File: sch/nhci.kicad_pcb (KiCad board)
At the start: 4 copper layers, 33 parts, among them IC1 74LVC8T245RHLRG4, IC2 74LVC8T245RHLRG4, IC3 74LVC8T245RHLRG4, IC4 74LVC8T245RHLRG4, IC5 74LVC8T245RHLRG4, IC6 MAX3421EEHJ+, SW1 SW_Push_Open, U1 PCMCIA_BOARD, U2 iCE40-HX8K-CT256, U3 N25Q032A13EF440F, Y1 ECS-5032MV-120-BM-TR

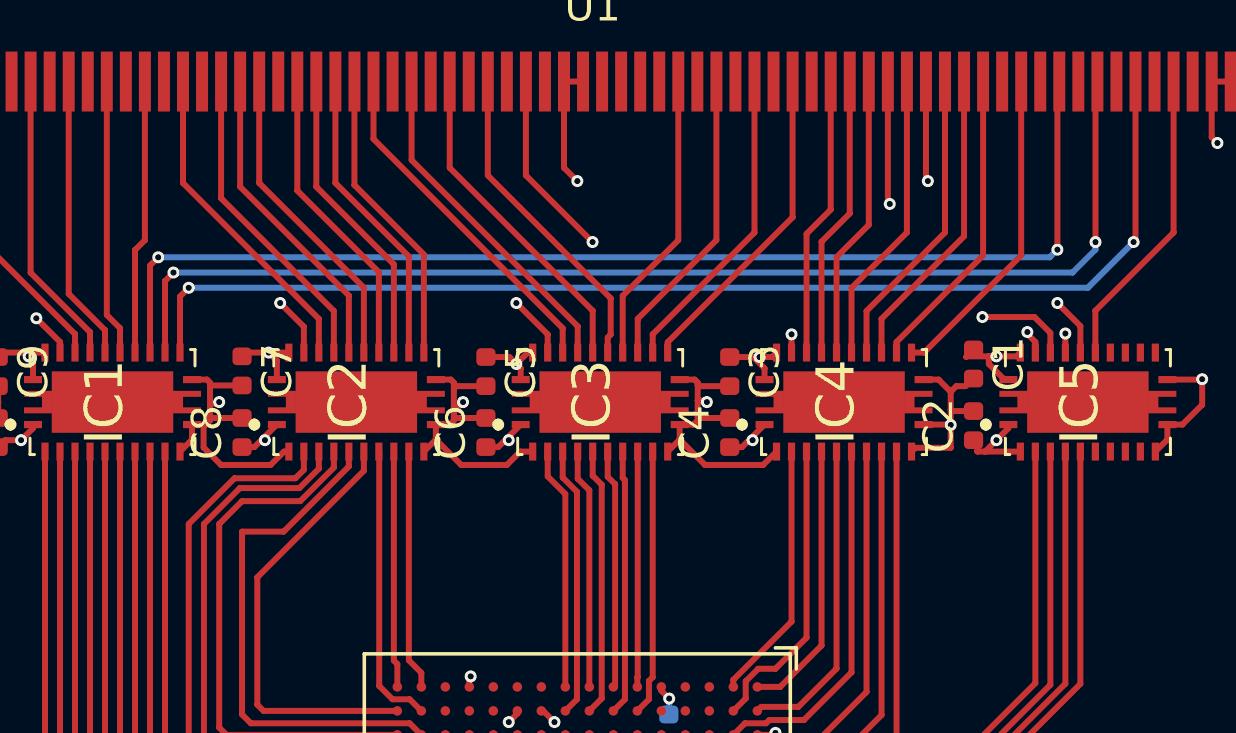
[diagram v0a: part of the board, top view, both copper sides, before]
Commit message: Add pullup resistors
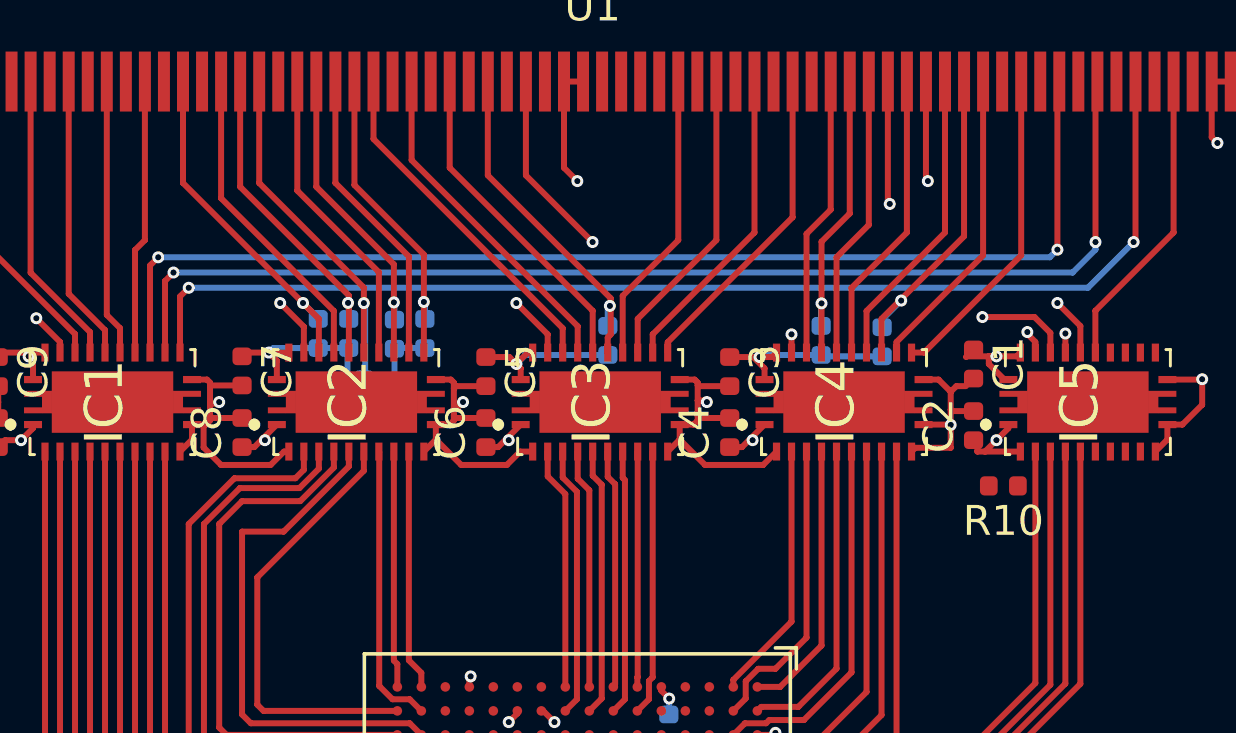
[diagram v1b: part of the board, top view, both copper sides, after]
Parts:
- added R10: 10k, Resistor_SMD:R_0402_1005Metric, F.Cu at (79.5, 111.8)
- added R2: 10k, Resistor_SMD:R_0402_1005Metric, B.Cu at (56.6, 106.7)
- added R3: 10k, Resistor_SMD:R_0402_1005Metric, B.Cu at (57.7, 106.7)
- added R4: 10k, Resistor_SMD:R_0402_1005Metric, B.Cu at (75.4, 107.0)
- added R5: 10k, Resistor_SMD:R_0402_1005Metric, B.Cu at (59.2, 106.7)
- added R6: 10k, Resistor_SMD:R_0402_1005Metric, B.Cu at (60.2, 106.7)
- added R7: 10k, Resistor_SMD:R_0402_1005Metric, B.Cu at (58.2, 108.7)
- added R8: 10k, Resistor_SMD:R_0402_1005Metric, B.Cu at (66.3, 106.9)
- added R9: 100k, Resistor_SMD:R_0402_1005Metric, B.Cu at (73.4, 106.9)
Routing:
- net +5V: track 57.8 -> 73.5 mm
- net /P_OE: track 10.5 -> 13.0 mm, vias 0 -> 1
- net /P_REG: track 10.2 -> 11.3 mm, vias 0 -> 1
- net /P_RESET: track 9.42 -> 10.2 mm, vias 0 -> 1
- net /P_CE1: track 10.9 -> 11.7 mm, vias 0 -> 1
- net /P_WE: track 10.8 -> 11.5 mm, vias 0 -> 1
- net /P_IORD: track 10.1 -> 10.7 mm, vias 0 -> 1
- net /P_IOWR: track 9.99 -> 10.6 mm, vias 0 -> 1
- net /P_CE2: track 10.5 -> 11.1 mm, vias 0 -> 1

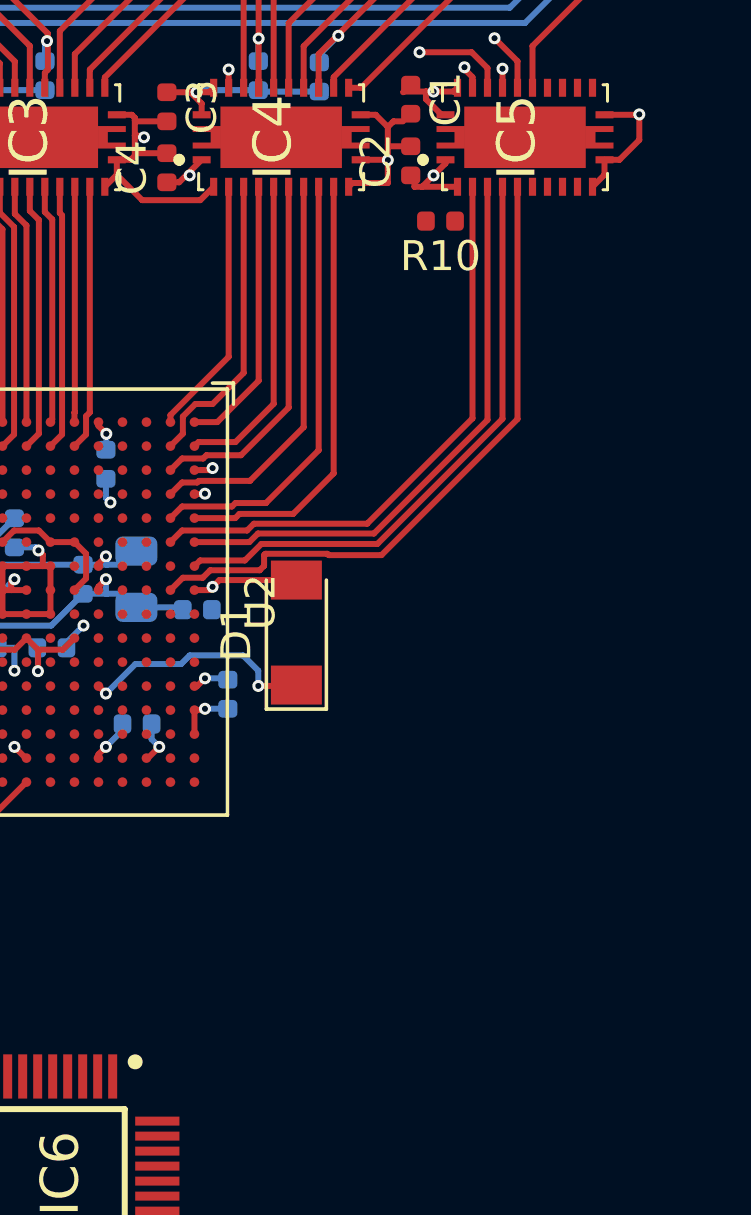
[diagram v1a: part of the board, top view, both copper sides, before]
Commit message: Add voltage regulator
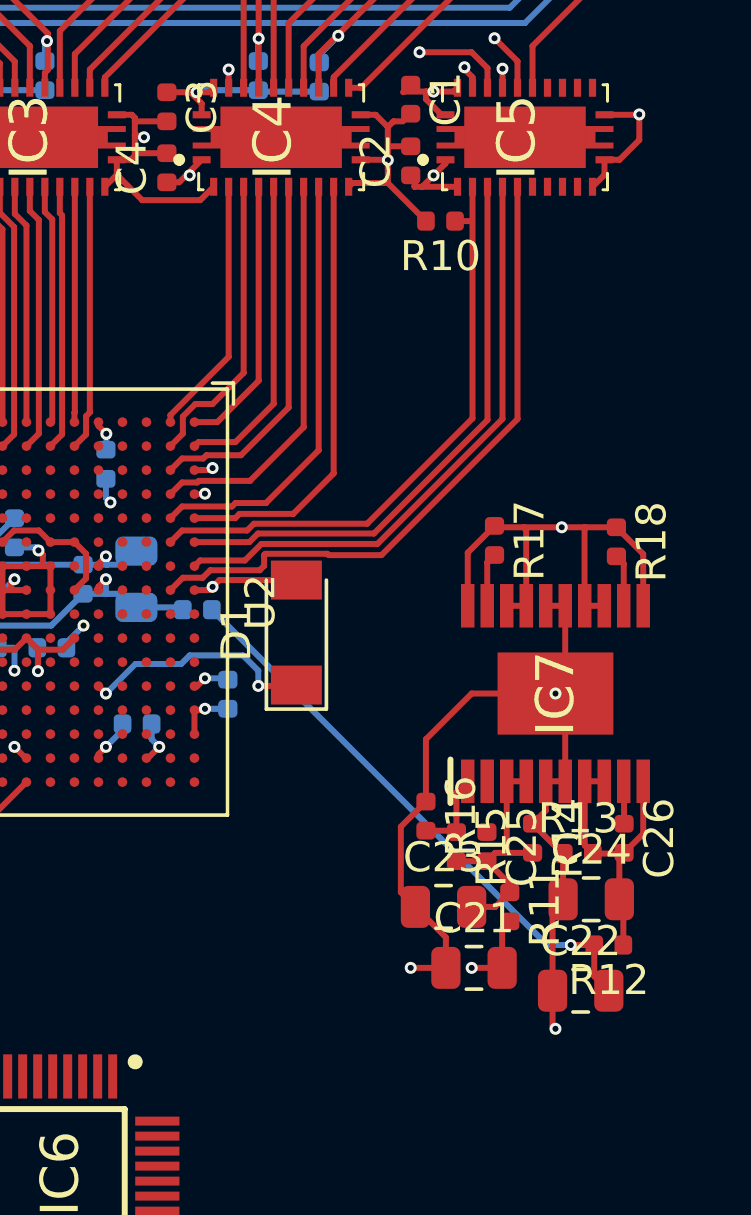
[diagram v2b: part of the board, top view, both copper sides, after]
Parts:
- added C21: 10uF, Capacitor_SMD:C_0805_2012Metric, F.Cu at (80.6, 136.7)
- added C22: 10uF, Capacitor_SMD:C_0805_2012Metric, F.Cu at (84.2, 137.4)
- added C23: 10uF, Capacitor_SMD:C_0805_2012Metric, F.Cu at (79.6, 134.6)
- added C24: 4.7uF, Capacitor_SMD:C_0805_2012Metric, F.Cu at (84.5, 134.4)
- added C25: 10nF, Capacitor_SMD:C_0402_1005Metric, F.Cu at (81.0, 132.6)
- added C26: 10nF, Capacitor_SMD:C_0402_1005Metric, F.Cu at (85.6, 132.3)
- added IC7: LT3030IFE#TRPBF, LT3030IFE#TRPBF:SOP65P640X120-21N, F.Cu at (83.3, 127.5)
- added R11: 0.1, Resistor_SMD:R_0402_1005Metric, F.Cu at (81.8, 134.6)
- added R12: 0.1, Resistor_SMD:R_0402_1005Metric, F.Cu at (85.1, 135.9)
- added R13: 100, Resistor_SMD:R_0402_1005Metric, F.Cu at (84.1, 132.8)
- added R14: 100, Resistor_SMD:R_0402_1005Metric, F.Cu at (82.5, 132.3)
- added R15: 357k, Resistor_SMD:R_0402_1005Metric, F.Cu at (80.0, 132.6)
- added R16: 210k, Resistor_SMD:R_0402_1005Metric, F.Cu at (79.0, 131.6)
- added R17: 1M, Resistor_SMD:R_0402_1005Metric, F.Cu at (81.3, 122.4)
- added R18: 1M, Resistor_SMD:R_0402_1005Metric, F.Cu at (85.3, 122.5)
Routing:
- net +5V: track 73.5 -> 106.9 mm, vias 6 -> 7
- net GND: track 80.7 -> 113.8 mm, vias 30 -> 33
- net +1V2: track 0.00 -> 19.1 mm, vias 0 -> 1
- net +3V3: track 95.8 -> 108.4 mm, vias 23 -> 24
- net Net-(C24-Pad2): track 0.00 -> 10.1 mm
- net Net-(C23-Pad2): track 0.00 -> 8.55 mm
- net Net-(IC7-Pad1): track 0.00 -> 2.88 mm
- net Net-(IC7-Pad19): track 0.00 -> 1.79 mm
- net Net-(IC7-Pad12): track 0.00 -> 1.75 mm
- net Net-(C26-Pad1): track 0.00 -> 1.42 mm
- net F_READY: track 19.5 -> 20.1 mm

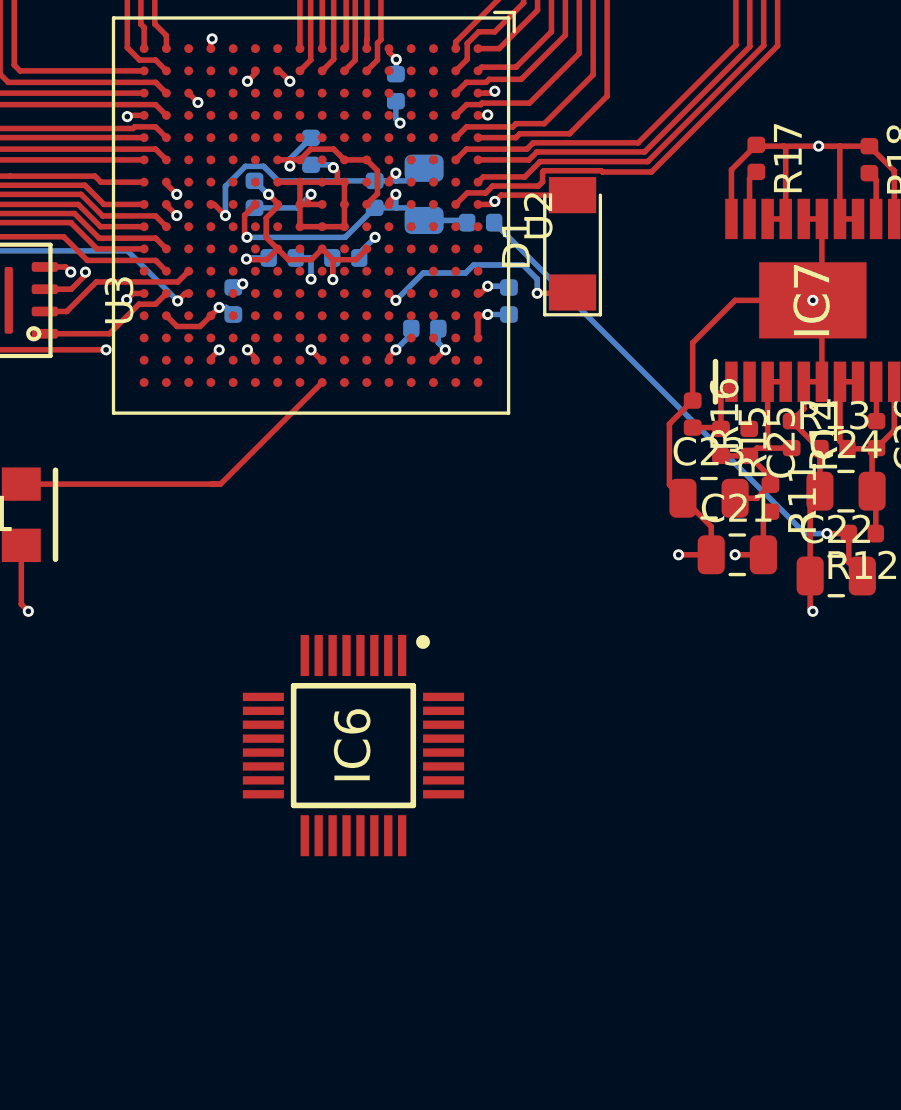
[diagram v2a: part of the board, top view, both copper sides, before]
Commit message: Add usb controller
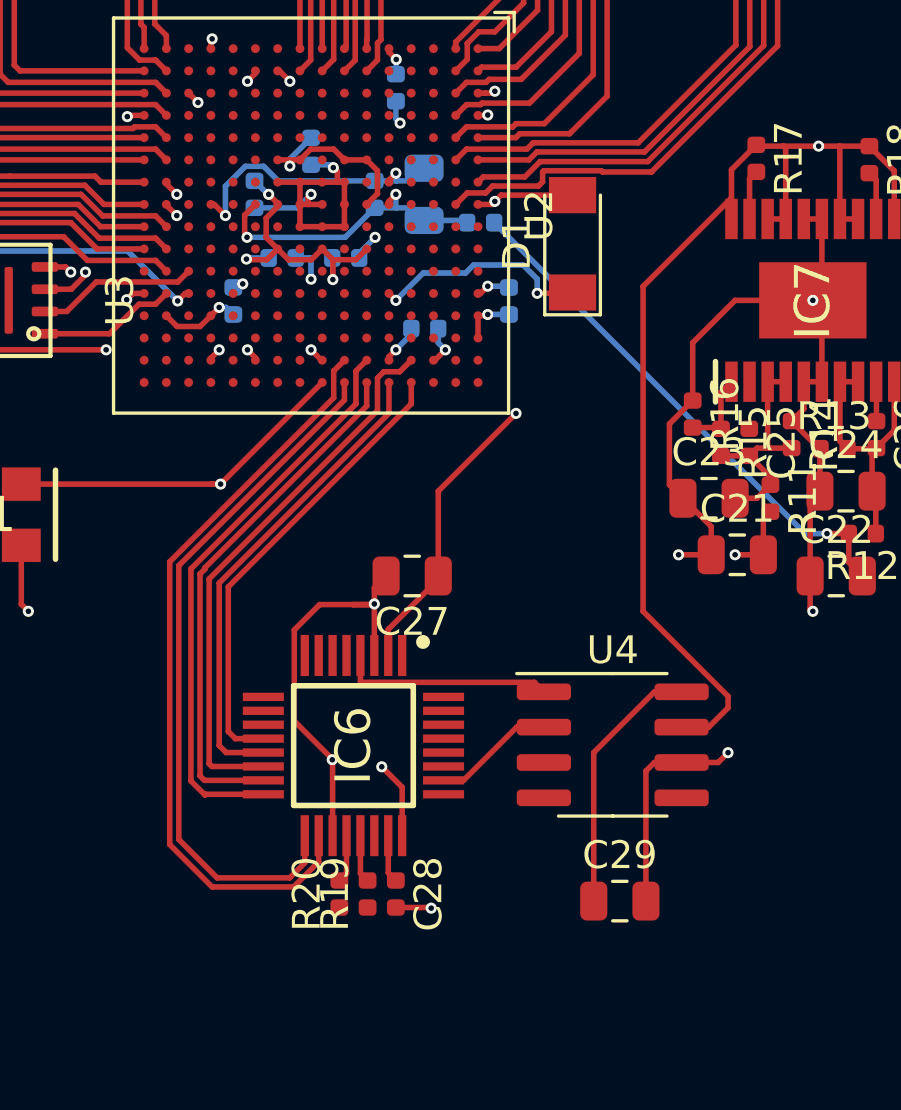
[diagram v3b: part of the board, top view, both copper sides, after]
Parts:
- added C27: 1uF, Capacitor_SMD:C_0805_2012Metric, F.Cu at (68.9, 137.4)
- added C28: 100nF, Capacitor_SMD:C_0402_1005Metric, F.Cu at (68.3, 148.8)
- added C29: 4.7uF, Capacitor_SMD:C_0805_2012Metric, F.Cu at (76.4, 149.1)
- added R19: 33, Resistor_SMD:R_0402_1005Metric, F.Cu at (67.3, 148.8)
- added R20: 33, Resistor_SMD:R_0402_1005Metric, F.Cu at (66.3, 148.8)
- added U4: LM3526M-H, Package_SO:SOIC-8_3.9x4.9mm_P1.27mm, F.Cu at (76.1, 143.5)
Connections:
- IC6 pad 12: Net-(IC6-Pad12) -> U_RES
- IC6 pad 13: Net-(IC6-Pad13) -> U_SCLK
- IC6 pad 14: Net-(IC6-Pad14) -> U_SS
- IC6 pad 15: Net-(IC6-Pad15) -> U_MISO
- IC6 pad 16: Net-(IC6-Pad16) -> U_MOSI
- IC6 pad 17: Net-(IC6-Pad17) -> U_GPX
- IC6 pad 18: Net-(IC6-Pad18) -> U_INT
- IC6 pad 19: Net-(IC6-Pad19) -> GND
- IC6 pad 2: Net-(IC6-Pad2) -> +3V3
- IC6 pad 23: Net-(IC6-Pad23) -> +3V3
- IC6 pad 24: Net-(IC6-Pad24) -> 12MHz
- IC6 pad 3: Net-(IC6-Pad3) -> GND
- U2 pad D15: Net-(U2-PadD15) -> U_SS
- U2 pad D16: Net-(U2-PadD16) -> U_RES
- U2 pad E16: Net-(U2-PadE16) -> U_SCLK
- U2 pad F15: Net-(U2-PadF15) -> U_MOSI
- U2 pad F16: Net-(U2-PadF16) -> U_MISO
- U2 pad G15: Net-(U2-PadG15) -> U_INT
- U2 pad G16: Net-(U2-PadG16) -> U_GPX
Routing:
- net U_INT: track 0.00 -> 27.3 mm
- net U_GPX: track 0.00 -> 25.2 mm
- net GND: track 113.8 -> 138.0 mm, vias 33 -> 37
- net +5V: track 106.9 -> 129.8 mm
- net U_MOSI: track 0.00 -> 20.6 mm
- net U_SS: track 0.00 -> 19.8 mm
- net U_MISO: track 0.00 -> 19.0 mm
- net U_SCLK: track 0.00 -> 17.3 mm
- net U_RES: track 0.00 -> 16.6 mm
- net 12MHz: track 12.6 -> 27.9 mm, vias 0 -> 2
- net +3V3: track 108.4 -> 120.7 mm, vias 24 -> 25
- net Net-(C29-Pad1): track 0.00 -> 9.40 mm
- net Net-(IC6-Pad4): track 0.00 -> 7.68 mm
- net Net-(IC6-Pad26): track 0.00 -> 4.40 mm
- net Net-(IC6-Pad20): track 0.00 -> 1.72 mm
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
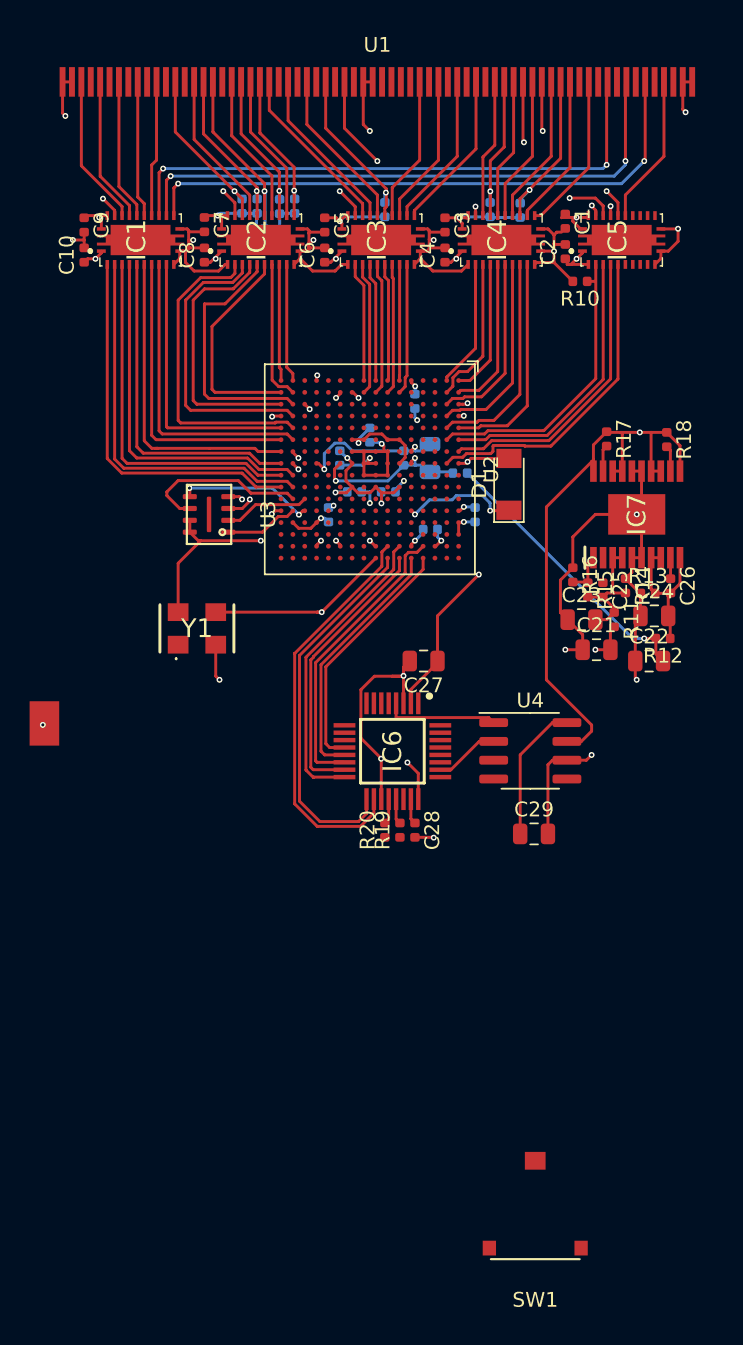
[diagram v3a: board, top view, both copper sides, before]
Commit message: Add solder jumper for non development board
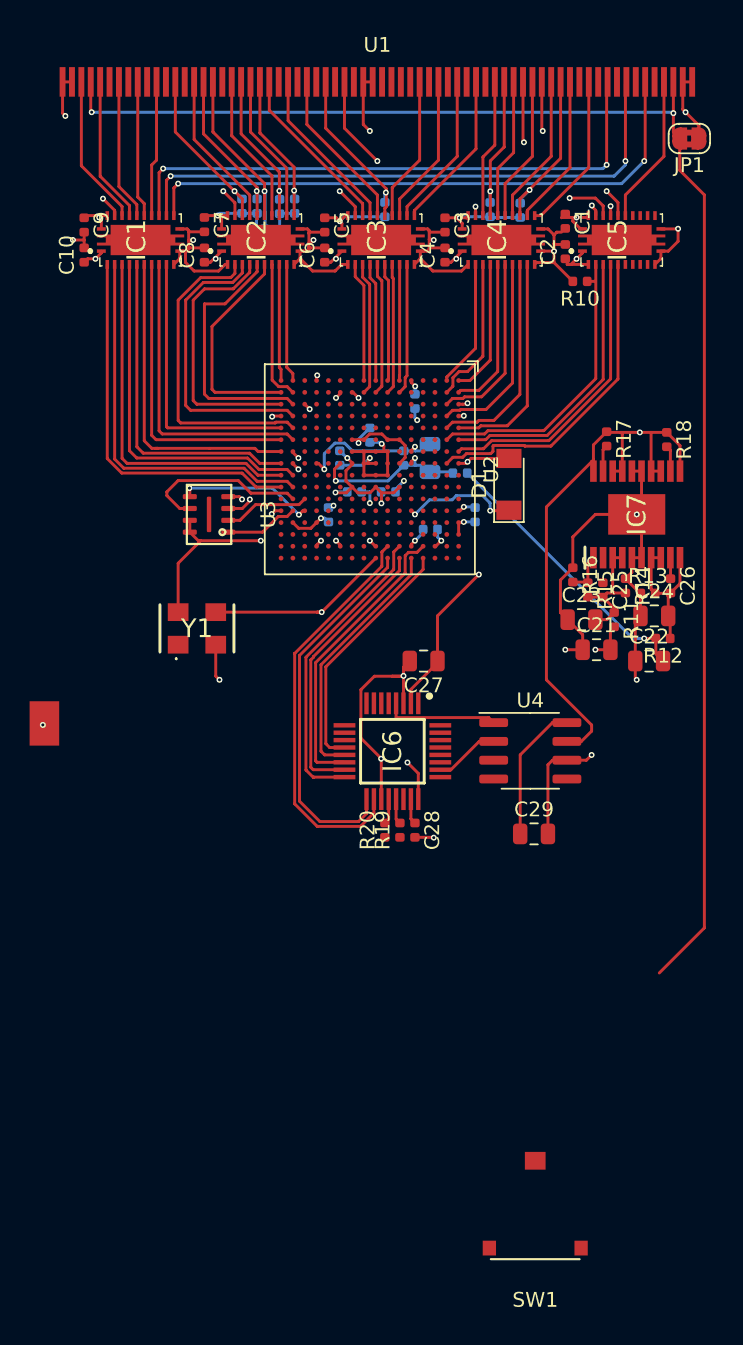
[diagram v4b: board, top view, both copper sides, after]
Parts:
- added JP1: SolderJumper_2_Bridged, Jumper:SolderJumper-2_P1.3mm_Bridged2Bar_RoundedPad1.0x1.5mm, F.Cu at (86.9, 102.1)
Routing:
- net Net-(JP1-Pad2): track 0.00 -> 103.8 mm, vias 0 -> 2
- net GND: track 138.0 -> 140.1 mm
